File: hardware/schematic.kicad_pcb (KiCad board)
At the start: 2 copper layers, 169.7 x 127.8 mm, 118 parts, among them J3 USB_C_Receptacle_USB2.0_16P

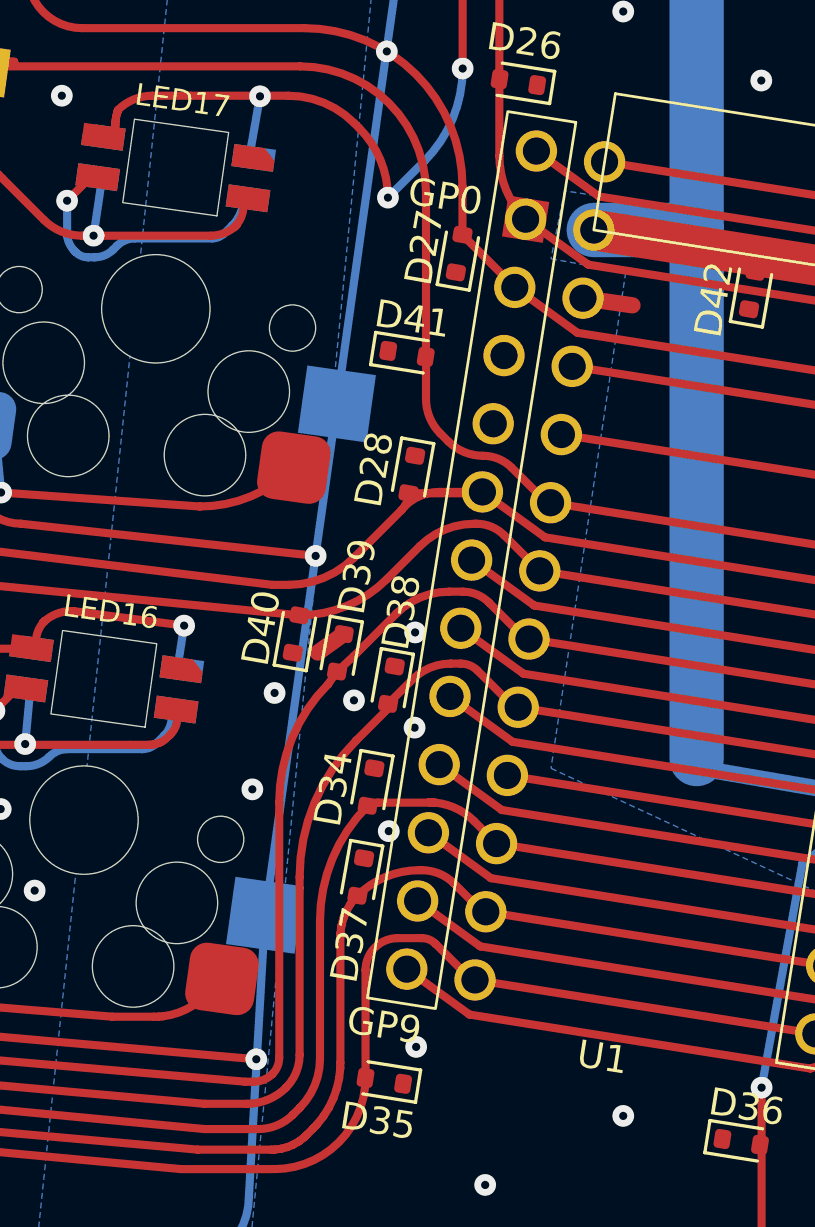
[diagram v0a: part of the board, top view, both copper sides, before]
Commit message: Add ergogen plate definition, move RP2040 footprint to project lib
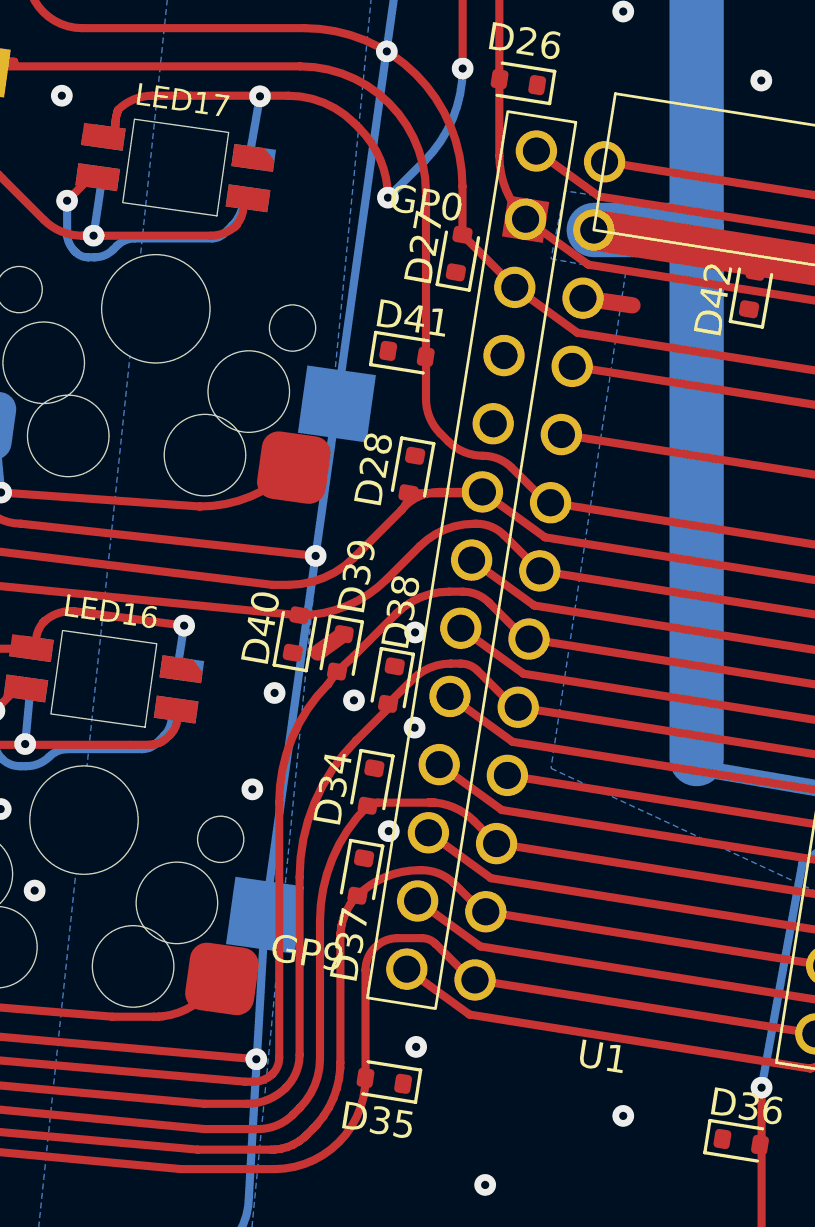
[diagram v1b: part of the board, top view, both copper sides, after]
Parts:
- U1: value ~ -> RP2040ProMicroCloneReversible; footprint RP2040ProMicroReversible:RP2040ProMicroCloneReversible -> footprints:RP2040ProMicroCloneReversible
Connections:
- U1 pad 0: /P0 -> (no net)
- U1 pad 1: /P1 -> (no net)
- U1 pad 10: /NC2 -> (no net)
- U1 pad 11: /NC1 -> (no net)
- U1 pad 2: /P2 -> (no net)
- U1 pad 20: /P20 -> (no net)
- U1 pad 21: /P21 -> (no net)
- U1 pad 22: /P22 -> (no net)
- U1 pad 23: /P23 -> (no net)
- U1 pad 26: /P26 -> (no net)
- U1 pad 27: /P27 -> (no net)
- U1 pad 28: /P28 -> (no net)
- U1 pad 29: /P29 -> (no net)
- U1 pad 3: /HAND -> (no net)
- U1 pad 3V3: /Vcc -> (no net)
- U1 pad 4: /NC3 -> (no net)
- U1 pad 5: /TXRX1 -> (no net)
- U1 pad 6: /TXRX2 -> (no net)
- U1 pad 7: /P7 -> (no net)
- U1 pad 8: /LED -> (no net)
- U1 pad 9: /P9 -> (no net)
- U1 pad G: GND -> (no net)
- U1 pad RST: /Reset -> (no net)
- U1 pad VRAW: Vraw -> (no net)
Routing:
- net Vraw: track 425.7 -> 444.1 mm
- net /NC2: track 18.4 -> 0.00 mm
- net /P0: track 232.3 -> 235.1 mm
- net GND: track 30.3 -> 27.5 mm
